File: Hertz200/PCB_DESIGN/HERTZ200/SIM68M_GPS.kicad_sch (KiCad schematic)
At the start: 14 parts

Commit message: Voltage_Level_Shifter
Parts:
- C?: value F -> 0.1uF
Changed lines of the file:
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@@
       (effects (font (size 1.27 1.27)) (justify left))
     )
-    (property "Value" "F" (id 1) (at 180.34 74.9362 0)
+    (property "Value" "0.1uF" (id 1) (at 180.34 74.9362 0)
       (effects (font (size 1.27 1.27)) (justify left))
     )

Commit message: schematics_Power_section
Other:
- moved on the sheet: C?

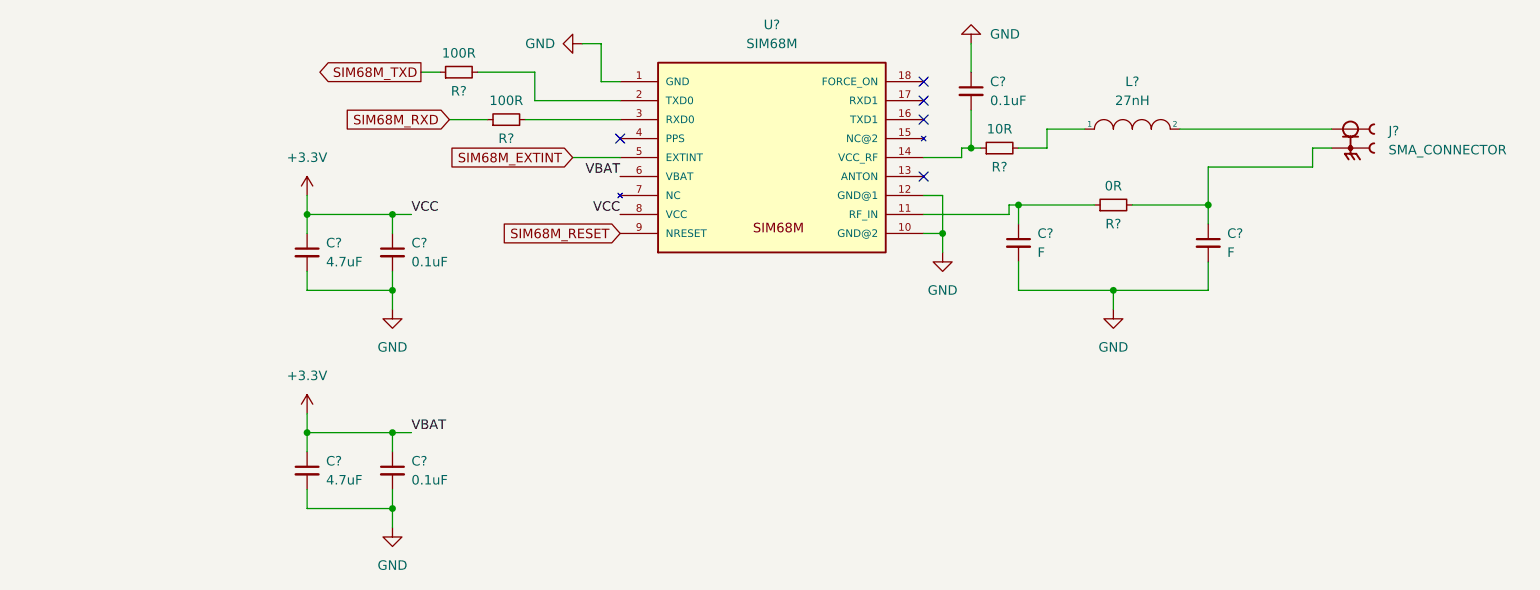
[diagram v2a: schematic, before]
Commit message: MCU-PIN-ASSIGNMENT
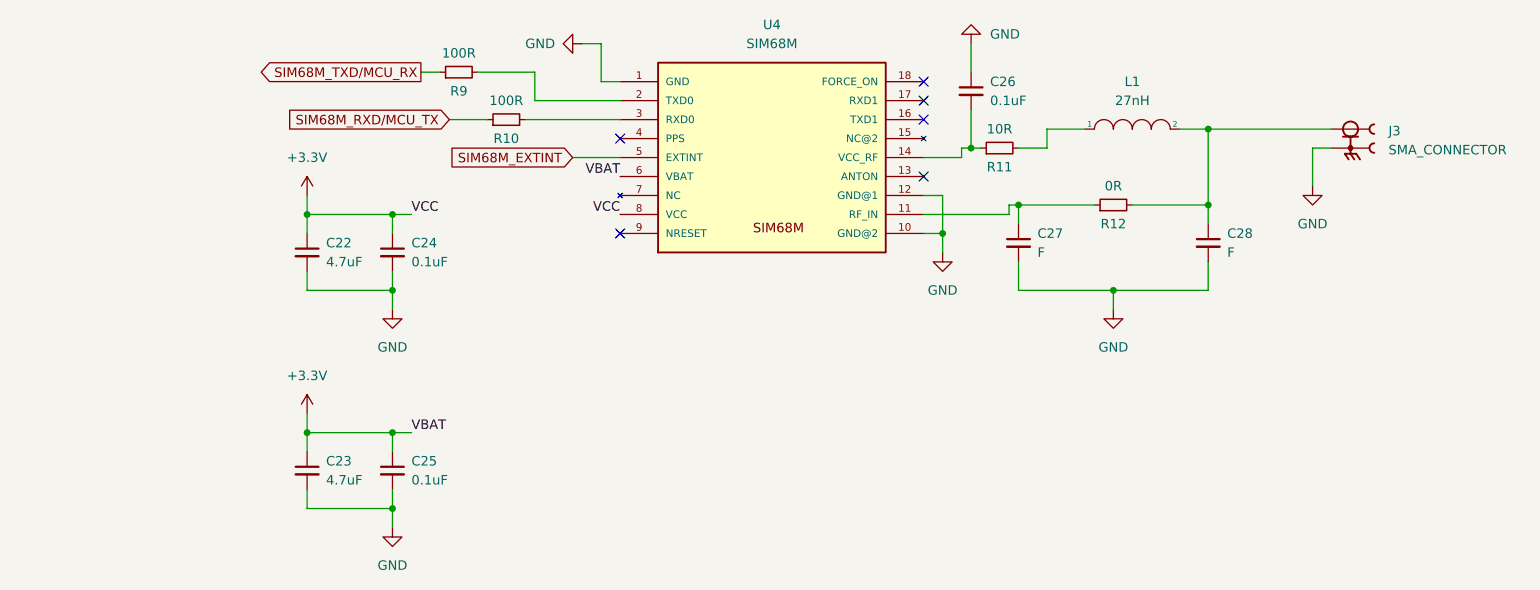
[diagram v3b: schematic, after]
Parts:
- gave numbers to parts that had none: 14
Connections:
- net GND: now also J3.G1, J3.G2, J3.G3, J3.G4
- net at J3.1, L1.2: now also C28.1, R12.2
- net SIM68M_RESET: no longer names the net of U4.9 (NRESET)
- net SIM68M_RXD renamed SIM68M_RXD/MCU_TX
- net SIM68M_TXD renamed SIM68M_TXD/MCU_RX
- no-connect marks 5 -> 6

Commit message: Component_selection
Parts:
- C22, C23, C24, C25, C26, C27, C28: footprint (none) -> Capacitor_SMD:C_0603_1608Metric
- J3: footprint LPRS_SMA_CONNECTOR -> (none)
- L1: footprint (none) -> Inductor_SMD:L_0603_1608Metric
- R10, R11, R12, R9: footprint (none) -> Resistor_SMD:R_0603_1608Metric
- U4: footprint SIM68M -> SIM68M:SIM68M
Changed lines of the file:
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@@
     (property "Reference" "R9" (id 0) (at 109.22 73.66 90))
     (property "Value" "100R" (id 1) (at 109.22 68.58 90))
-    (property "Footprint" "" (id 2) (at 109.22 71.12 0)
+    (property "Footprint" "Resistor_SMD:R_0603_1608Metric" (id 2) (at 109.22 71.12 0)
       (effects (font (size 1.27 1.27)) hide)
     )
@@
     (property "Reference" "L1" (id 0) (at 199.39 72.39 0))
     (property "Value" "27nH" (id 1) (at 199.39 74.93 0))
-    (property "Footprint" "" (id 2) (at 199.39 78.74 0)
+    (property "Footprint" "Inductor_SMD:L_0603_1608Metric" (id 2) (at 199.39 78.74 0)
       (effects (font (size 1.27 1.27)) hide)
     )
@@
     (property "Reference" "R10" (id 0) (at 115.57 80.01 90))
     (property "Value" "100R" (id 1) (at 115.57 74.93 90))
-    (property "Footprint" "" (id 2) (at 115.57 77.47 0)
+    (property "Footprint" "Resistor_SMD:R_0603_1608Metric" (id 2) (at 115.57 77.47 0)
       (effects (font (size 1.27 1.27)) hide)
     )
@@
       (effects (font (size 1.27 1.27)) (justify left))
     )
-    (property "Footprint" "" (id 2) (at 184.15 93.98 0)
+    (property "Footprint" "Capacitor_SMD:C_0603_1608Metric" (id 2) (at 184.15 93.98 0)
       (effects (font (size 1.27 1.27)) hide)
     )
@@
       (effects (font (size 1.27 1.27)) (justify left))
     )
-    (property "Footprint" "" (id 2) (at 209.55 93.98 0)
+    (property "Footprint" "Capacitor_SMD:C_0603_1608Metric" (id 2) (at 209.55 93.98 0)
       (effects (font (size 1.27 1.27)) hide)
     )
@@
       (effects (font (size 1.27 1.27)) (justify right))
     )
-    (property "Footprint" "LPRS_SMA_CONNECTOR" (id 2) (at 228.6 78.74 0)
+    (property "Footprint" "" (id 2) (at 228.6 78.74 0)
       (effects (font (size 1.27 1.27)) (justify left bottom) hide)
     )
@@
     (property "Reference" "U4" (id 0) (at 151.13 64.77 0))
     (property "Value" "SIM68M" (id 1) (at 151.13 67.31 0))
-    (property "Footprint" "SIM68M" (id 2) (at 151.13 85.09 0)
+    (property "Footprint" "SIM68M:SIM68M" (id 2) (at 151.13 85.09 0)
       (effects (font (size 1.27 1.27)) (justify left bottom) hide)
     )
@@
       (effects (font (size 1.27 1.27)) (justify left))
     )
-    (property "Footprint" "" (id 2) (at 100.33 124.46 0)
+    (property "Footprint" "Capacitor_SMD:C_0603_1608Metric" (id 2) (at 100.33 124.46 0)
       (effects (font (size 1.27 1.27)) hide)
     )
@@
       (effects (font (size 1.27 1.27)) (justify left))
     )
-    (property "Footprint" "" (id 2) (at 88.9 95.25 0)
+    (property "Footprint" "Capacitor_SMD:C_0603_1608Metric" (id 2) (at 88.9 95.25 0)
       (effects (font (size 1.27 1.27)) hide)
     )
@@
       (effects (font (size 1.27 1.27)) (justify left))
     )
-    (property "Footprint" "" (id 2) (at 88.9 124.46 0)
+    (property "Footprint" "Capacitor_SMD:C_0603_1608Metric" (id 2) (at 88.9 124.46 0)
       (effects (font (size 1.27 1.27)) hide)
     )
@@
       (effects (font (size 1.27 1.27)) (justify left))
     )
-    (property "Footprint" "" (id 2) (at 177.8 73.66 0)
+    (property "Footprint" "Capacitor_SMD:C_0603_1608Metric" (id 2) (at 177.8 73.66 0)
       (effects (font (size 1.27 1.27)) hide)
     )
@@
     (property "Reference" "R12" (id 0) (at 196.85 91.44 90))
     (property "Value" "0R" (id 1) (at 196.85 86.36 90))
-    (property "Footprint" "" (id 2) (at 196.85 88.9 0)
+    (property "Footprint" "Resistor_SMD:R_0603_1608Metric" (id 2) (at 196.85 88.9 0)
       (effects (font (size 1.27 1.27)) hide)
     )
@@
       (effects (font (size 1.27 1.27)) (justify left))
     )
-    (property "Footprint" "" (id 2) (at 100.33 95.25 0)
+    (property "Footprint" "Capacitor_SMD:C_0603_1608Metric" (id 2) (at 100.33 95.25 0)
       (effects (font (size 1.27 1.27)) hide)
     )
@@
     (property "Reference" "R11" (id 0) (at 181.61 83.82 90))
     (property "Value" "10R" (id 1) (at 181.61 78.74 90))
-    (property "Footprint" "" (id 2) (at 181.61 81.28 0)
-      (effects (font (size 1.27 1.27)) hide)
-    )
+    (property "Footprint" "Resistor_SMD:R_0603_1608Metric" (id 2) (at 181.61 81.28 0)
+      (effects (font (size 1.27 1.27)) hide)
+    )

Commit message: layout
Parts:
- J3: footprint (none) -> SMA_CONNECTOR:LPRS_SMA_CONNECTOR
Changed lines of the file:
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@@
       (effects (font (size 1.27 1.27)) (justify right))
     )
-    (property "Footprint" "" (id 2) (at 228.6 78.74 0)
+    (property "Footprint" "SMA_CONNECTOR:LPRS_SMA_CONNECTOR" (id 2) (at 228.6 78.74 0)
       (effects (font (size 1.27 1.27)) (justify left bottom) hide)
     )

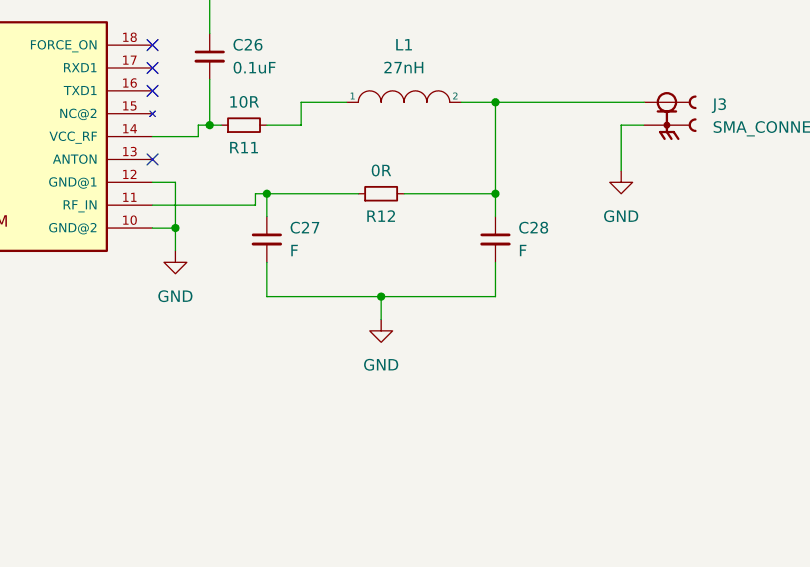
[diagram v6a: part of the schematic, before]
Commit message: TEMPERATURE SENSOR ROUTING
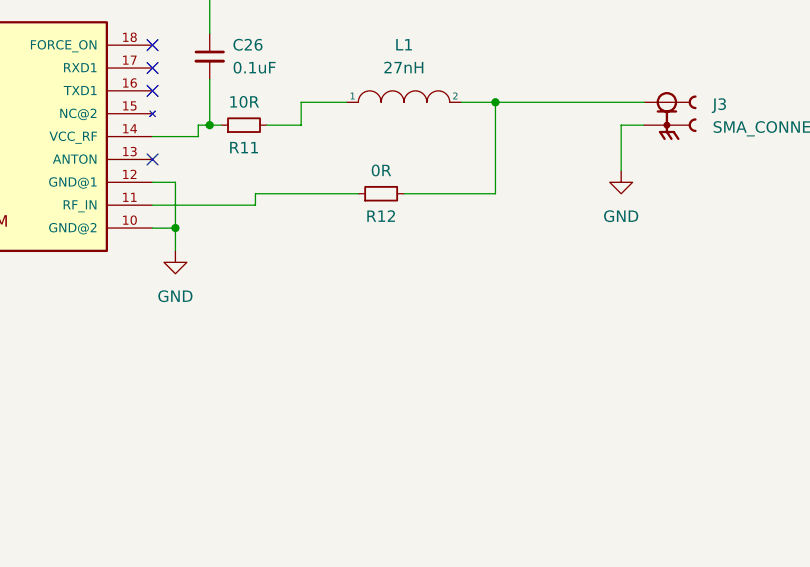
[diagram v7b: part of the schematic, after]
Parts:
- removed C27, C28: F, Capacitor_SMD:C_0603_1608Metric, symbol Device:C_Small
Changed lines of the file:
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@@
   (junction (at 173.99 92.71) (diameter 0) (color 0 0 0 0)
   )
-  (junction (at 196.85 100.33) (diameter 0) (color 0 0 0 0)
-  )
   (junction (at 88.9 119.38) (diameter 0) (color 0 0 0 0)
-  )
-  (junction (at 184.15 88.9) (diameter 0) (color 0 0 0 0)
-  )
-  (junction (at 209.55 88.9) (diameter 0) (color 0 0 0 0)
   )
   (junction (at 209.55 78.74) (diameter 0) (color 0 0 0 0)
@@
     (stroke (width 0) (type default) (color 0 0 0 0))
   )
-  (wire (pts (xy 209.55 100.33) (xy 209.55 96.52))
-    (stroke (width 0) (type default) (color 0 0 0 0))
-  )
   (wire (pts (xy 88.9 116.84) (xy 88.9 119.38))
     (stroke (width 0) (type default) (color 0 0 0 0))
@@
     (stroke (width 0) (type default) (color 0 0 0 0))
   )
-  (wire (pts (xy 182.88 88.9) (xy 184.15 88.9))
-    (stroke (width 0) (type default) (color 0 0 0 0))
-  )
   (wire (pts (xy 100.33 90.17) (xy 102.87 90.17))
     (stroke (width 0) (type default) (color 0 0 0 0))
@@
     (stroke (width 0) (type default) (color 0 0 0 0))
   )
-  (wire (pts (xy 196.85 100.33) (xy 196.85 102.87))
-    (stroke (width 0) (type default) (color 0 0 0 0))
-  )
   (wire (pts (xy 128.27 72.39) (xy 128.27 67.31))
     (stroke (width 0) (type default) (color 0 0 0 0))
@@
     (stroke (width 0) (type default) (color 0 0 0 0))
   )
-  (wire (pts (xy 184.15 100.33) (xy 196.85 100.33))
-    (stroke (width 0) (type default) (color 0 0 0 0))
-  )
   (wire (pts (xy 118.11 77.47) (xy 130.81 77.47))
     (stroke (width 0) (type default) (color 0 0 0 0))
@@
     (stroke (width 0) (type default) (color 0 0 0 0))
   )
-  (wire (pts (xy 196.85 100.33) (xy 209.55 100.33))
-    (stroke (width 0) (type default) (color 0 0 0 0))
-  )
-  (wire (pts (xy 184.15 91.44) (xy 184.15 88.9))
-    (stroke (width 0) (type default) (color 0 0 0 0))
-  )
   (wire (pts (xy 111.76 71.12) (xy 119.38 71.12))
     (stroke (width 0) (type default) (color 0 0 0 0))
@@
     (stroke (width 0) (type default) (color 0 0 0 0))
   )
-  (wire (pts (xy 209.55 88.9) (xy 209.55 91.44))
-    (stroke (width 0) (type default) (color 0 0 0 0))
-  )
   (wire (pts (xy 176.53 82.55) (xy 176.53 81.28))
     (stroke (width 0) (type default) (color 0 0 0 0))
@@
     (stroke (width 0) (type default) (color 0 0 0 0))
   )
-  (wire (pts (xy 184.15 88.9) (xy 194.31 88.9))
+  (wire (pts (xy 182.88 88.9) (xy 194.31 88.9))
     (stroke (width 0) (type default) (color 0 0 0 0))
   )
@@
   )
   (wire (pts (xy 100.33 100.33) (xy 100.33 97.79))
-    (stroke (width 0) (type default) (color 0 0 0 0))
-  )
-  (wire (pts (xy 184.15 96.52) (xy 184.15 100.33))
     (stroke (width 0) (type default) (color 0 0 0 0))
   )
@@
     )
     (property "Datasheet" "~" (id 3) (at 115.57 77.47 0)
-      (effects (font (size 1.27 1.27)) hide)
-    )
-    (pin "1")
-    (pin "2")
-  )
-  (symbol (lib_id "Device:C_Small") (at 184.15 93.98 0) (unit 1)
-    (in_bom yes) (on_board yes) (fields_autoplaced)
-    (property "Reference" "C27" (id 0) (at 186.69 92.7162 0)
-      (effects (font (size 1.27 1.27)) (justify left))
-    )
-    (property "Value" "F" (id 1) (at 186.69 95.2562 0)
-      (effects (font (size 1.27 1.27)) (justify left))
-    )
-    (property "Footprint" "Capacitor_SMD:C_0603_1608Metric" (id 2) (at 184.15 93.98 0)
-      (effects (font (size 1.27 1.27)) hide)
-    )
-    (property "Datasheet" "~" (id 3) (at 184.15 93.98 0)
-      (effects (font (size 1.27 1.27)) hide)
-    )
-    (pin "1")
-    (pin "2")
-  )
-  (symbol (lib_id "Device:C_Small") (at 209.55 93.98 0) (unit 1)
-    (in_bom yes) (on_board yes) (fields_autoplaced)
-    (property "Reference" "C28" (id 0) (at 212.09 92.7162 0)
-      (effects (font (size 1.27 1.27)) (justify left))
-    )
-    (property "Value" "F" (id 1) (at 212.09 95.2562 0)
-      (effects (font (size 1.27 1.27)) (justify left))
-    )
-    (property "Footprint" "Capacitor_SMD:C_0603_1608Metric" (id 2) (at 209.55 93.98 0)
-      (effects (font (size 1.27 1.27)) hide)
-    )
-    (property "Datasheet" "~" (id 3) (at 209.55 93.98 0)
       (effects (font (size 1.27 1.27)) hide)
     )
@@
     (pin "2")
   )
-  (symbol (lib_id "power:GND") (at 196.85 102.87 0) (unit 1)
-    (in_bom yes) (on_board yes) (fields_autoplaced)
-    (property "Reference" "#PWR034" (id 0) (at 196.85 109.22 0)
-      (effects (font (size 1.27 1.27)) hide)
-    )
-    (property "Value" "GND" (id 1) (at 196.85 107.95 0))
-    (property "Footprint" "" (id 2) (at 196.85 102.87 0)
-      (effects (font (size 1.27 1.27)) hide)
-    )
-    (property "Datasheet" "" (id 3) (at 196.85 102.87 0)
-      (effects (font (size 1.27 1.27)) hide)
-    )
-    (pin "1")
-  )
   (symbol (lib_id "power:GND") (at 125.73 67.31 270) (unit 1)
